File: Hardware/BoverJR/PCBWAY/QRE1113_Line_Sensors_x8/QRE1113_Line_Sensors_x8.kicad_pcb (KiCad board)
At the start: 2 copper layers, 70 x 17 mm, 29 parts, among them J1 Conn_01x10_Pin, U1 QRE1113GR, U2 QRE1113GR, U3 QRE1113GR, U4 QRE1113GR, U5 QRE1113GR, U6 QRE1113GR, U7 QRE1113GR, U8 QRE1113GR

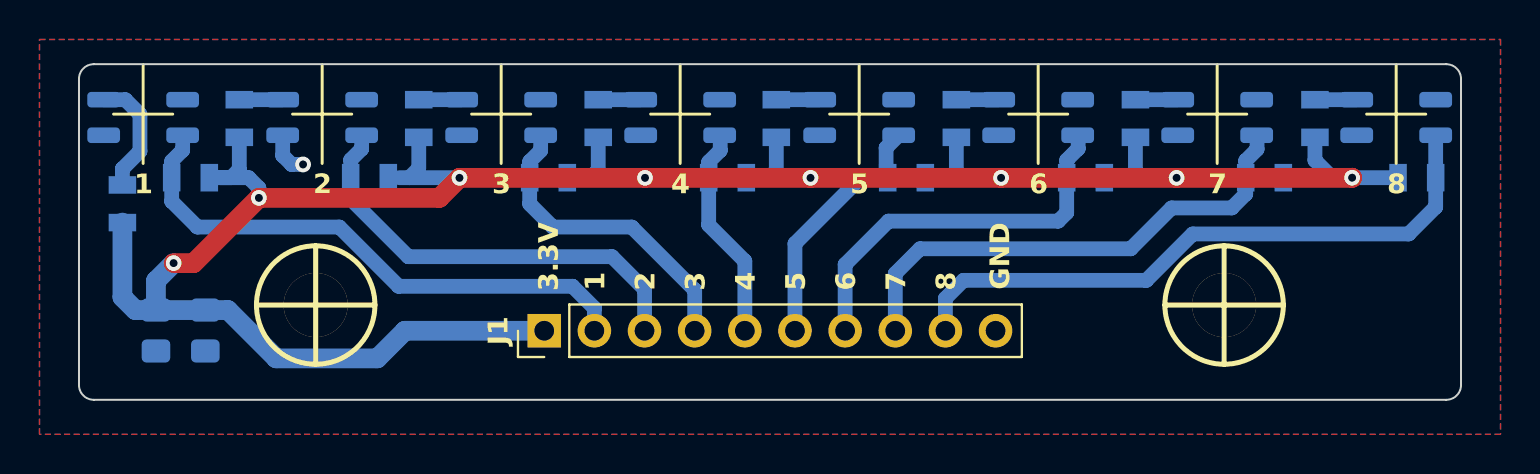
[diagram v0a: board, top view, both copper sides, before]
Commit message: esperando verificacion de pcbway ya cargue 6 gerber
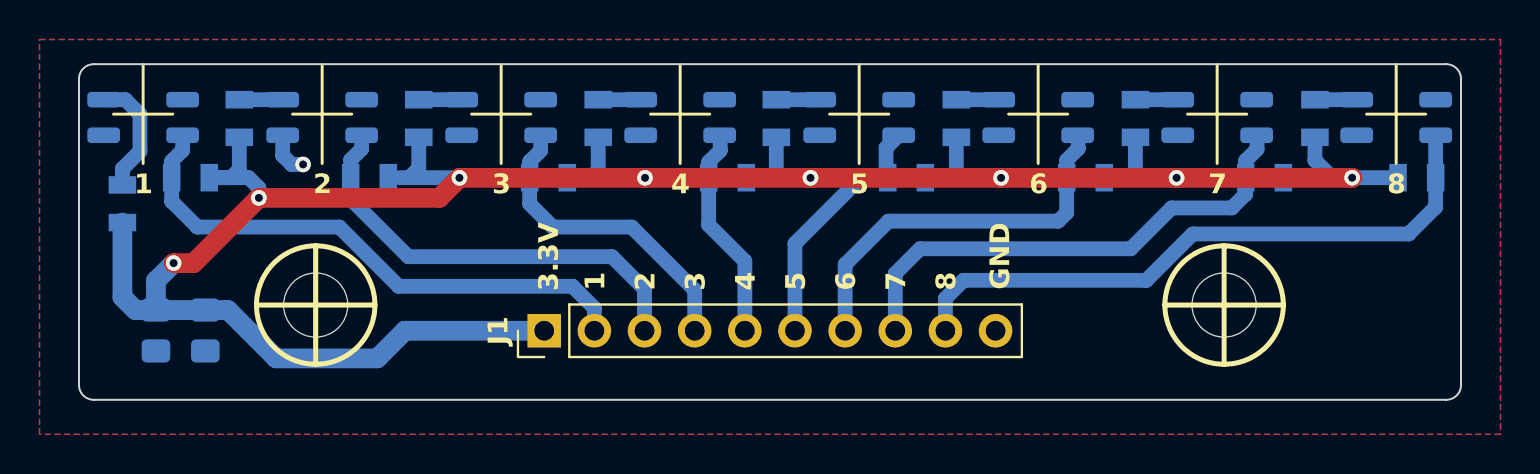
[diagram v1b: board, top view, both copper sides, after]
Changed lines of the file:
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@@
     (pad_to_mask_clearance 0)
     (pcbplotparams
-      (layerselection 0x0000000_fffffffe)
+      (layerselection 0x00010fc_ffffffff)
       (plot_on_all_layers_selection 0x0001000_00000000)
       (disableapertmacros false)
@@
       (psnegative false)
       (psa4output false)
-      (plotreference false)
+      (plotreference true)
       (plotvalue false)
       (plotinvisibletext false)
       (sketchpadsonfab false)
       (subtractmaskfromsilk false)
-      (outputformat 5)
+      (outputformat 1)
       (mirror false)
-      (drillshape 1)
+      (drillshape 0)
       (scaleselection 1)
-      (outputdirectory "")
+      (outputdirectory "../gerber/QREX8/")
     )
   )
@@
     (fp_circle (center 0 0) (end 3 0)
       (stroke (width 0.254) (type solid)) (fill none) (layer "F.SilkS"))
-    (pad "1" thru_hole circle (at 0 0) (size 3.25 3.25) (drill 3.25) (layers "*.Cu" "F.SilkS"))
+    (pad "1" thru_hole circle (at 0 0) (size 3.25 3.25) (drill 3.25) (layers "*.Mask"))
     (model "D:/APPS Mauri/KiCad Carpetas/EESTN5 - Librerias Kicad/EESTN5.3dshapes/Separador_M3_5mm.wrl"
       (offset (xyz 0 0 0))
@@
     (fp_circle (center 0 0) (end 3 0)
       (stroke (width 0.254) (type solid)) (fill none) (layer "F.SilkS"))
-    (pad "1" thru_hole circle (at 0 0) (size 3.25 3.25) (drill 3.25) (layers "*.Cu" "F.SilkS"))
+    (pad "1" thru_hole circle (at 0 0) (size 3.25 3.25) (drill 3.25) (layers "*.Mask"))
     (model "D:/APPS Mauri/KiCad Carpetas/EESTN5 - Librerias Kicad/EESTN5.3dshapes/Separador_M3_5mm.wrl"
       (offset (xyz 0 0 0))
@@
     (fp_line (start 1 0.625) (end 1 -0.625)
       (stroke (width 0.1) (type solid)) (layer "B.Fab"))
-    (pad "1" smd roundrect (at -1.0375 0 270) (size 1.175 1.45) (layers "B.Cu" "B.Paste" "B.Mask") (roundrect_rratio 0.212766)
-      (net 2 "+3V3") (pintype "passive"))
-    (pad "2" smd roundrect (at 1.0375 0 270) (size 1.175 1.45) (layers "B.Cu" "B.Paste" "B.Mask") (roundrect_rratio 0.212766)
+    (pad "1" smd roundrect (at -1.0375 0 270) (size 1.175 1.45) (layers "B.Cu" "B.Paste" "B.Mask") (roundrect_rratio 0.2127659574)
+      (net 2 "+3V3") (pintype "passive"))
+    (pad "2" smd roundrect (at 1.0375 0 270) (size 1.175 1.45) (layers "B.Cu" "B.Paste" "B.Mask") (roundrect_rratio 0.2127659574)
       (net 1 "GND") (pintype "passive"))
     (model "${KICAD6_3DMODEL_DIR}/Capacitor_SMD.3dshapes/C_0805_2012Metric.wrl"
@@
     (fp_line (start 1 0.625) (end 1 -0.625)
       (stroke (width 0.1) (type solid)) (layer "B.Fab"))
-    (pad "1" smd roundrect (at -1.0375 0 270) (size 1.175 1.45) (layers "B.Cu" "B.Paste" "B.Mask") (roundrect_rratio 0.212766)
-      (net 2 "+3V3") (pintype "passive"))
-    (pad "2" smd roundrect (at 1.0375 0 270) (size 1.175 1.45) (layers "B.Cu" "B.Paste" "B.Mask") (roundrect_rratio 0.212766)
+    (pad "1" smd roundrect (at -1.0375 0 270) (size 1.175 1.45) (layers "B.Cu" "B.Paste" "B.Mask") (roundrect_rratio 0.2127659574)
+      (net 2 "+3V3") (pintype "passive"))
+    (pad "2" smd roundrect (at 1.0375 0 270) (size 1.175 1.45) (layers "B.Cu" "B.Paste" "B.Mask") (roundrect_rratio 0.2127659574)
       (net 1 "GND") (pintype "passive"))
     (model "${KICAD6_3DMODEL_DIR}/Capacitor_SMD.3dshapes/C_0805_2012Metric.wrl"
